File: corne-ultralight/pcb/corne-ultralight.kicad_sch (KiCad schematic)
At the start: 102 parts, among them J2 OLED, J7 OLED, SW1 SW_PUSH, SW10 SW_PUSH, SW11 SW_PUSH, SW12 SW_PUSH, SW13 SW_PUSH, SW14 SW_PUSH, SW15 SW_PUSH, SW16 SW_PUSH, SW17 SW_PUSH, SW18 SW_PUSH, SW19 SW_PUSH, SW2 SW_PUSH, SW20 SW_PUSH, SW21 SW_PUSH, SW22 SW_PUSH, SW23 SW_PUSH, SW24 SW_PUSH, SW25 SW_PUSH, SW26 SW_PUSH, SW27 SW_PUSH, SW28 SW_PUSH, SW29 SW_PUSH, SW3 SW_PUSH, SW30 SW_PUSH, SW31 SW_PUSH, SW32 SW_PUSH, SW33 SW_PUSH, SW34 SW_PUSH, SW35 SW_PUSH, SW36 SW_PUSH, SW37 SW_PUSH, SW38 SW_PUSH, SW39 SW_PUSH, SW4 SW_PUSH, SW40 SW_PUSH, SW41 SW_PUSH, SW42 SW_PUSH, SW5 SW_PUSH, SW6 SW_PUSH, SW7 SW_PUSH, SW8 SW_PUSH, SW9 SW_PUSH, U1 ProMicro, U2 ProMicro

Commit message: Right half changed to hotswaps
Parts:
- SW22, SW23, SW24, SW25, SW26, SW27, SW28, SW29, SW30, SW31, SW32, SW33, SW34, SW35, SW36, SW37, SW38, SW39, SW40, SW41: footprint gateron-ks27:gateron-ks27-choc-v1 -> kbd:CherryMX_Choc_Hotswap_BACKONLY_FLIPPED
- SW42: footprint gateron-ks27:gateron-ks27-choc-v1-1.5u -> kbd:CherryMX_Choc_Hotswap_1.5u_BACKONLY_FLIPPED

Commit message: Fixed flipped footprints
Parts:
- SW22, SW23, SW24, SW25, SW26, SW27, SW28, SW29, SW30, SW31, SW32, SW33, SW34, SW35, SW36, SW37, SW38, SW39, SW40, SW41: footprint kbd:CherryMX_Choc_Hotswap_BACKONLY_FLIPPED -> kbd:CherryMX_Choc_Hotswap_BACKONLY
- SW42: footprint kbd:CherryMX_Choc_Hotswap_1.5u_BACKONLY_FLIPPED -> kbd:CherryMX_Choc_Hotswap_1.5u_BACKONLY

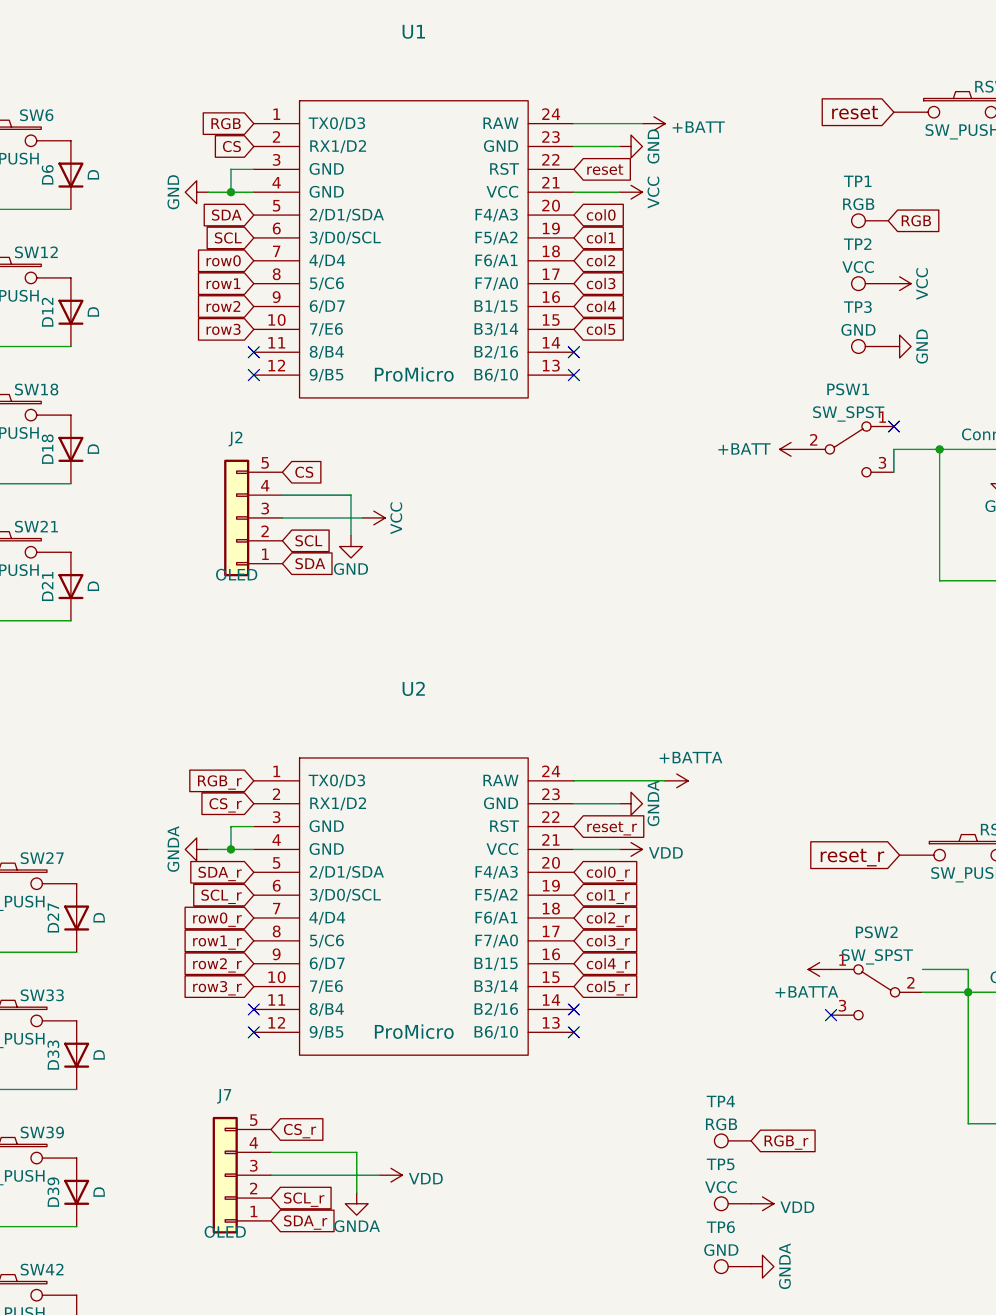
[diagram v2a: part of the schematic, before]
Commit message: Added XIAO footprint
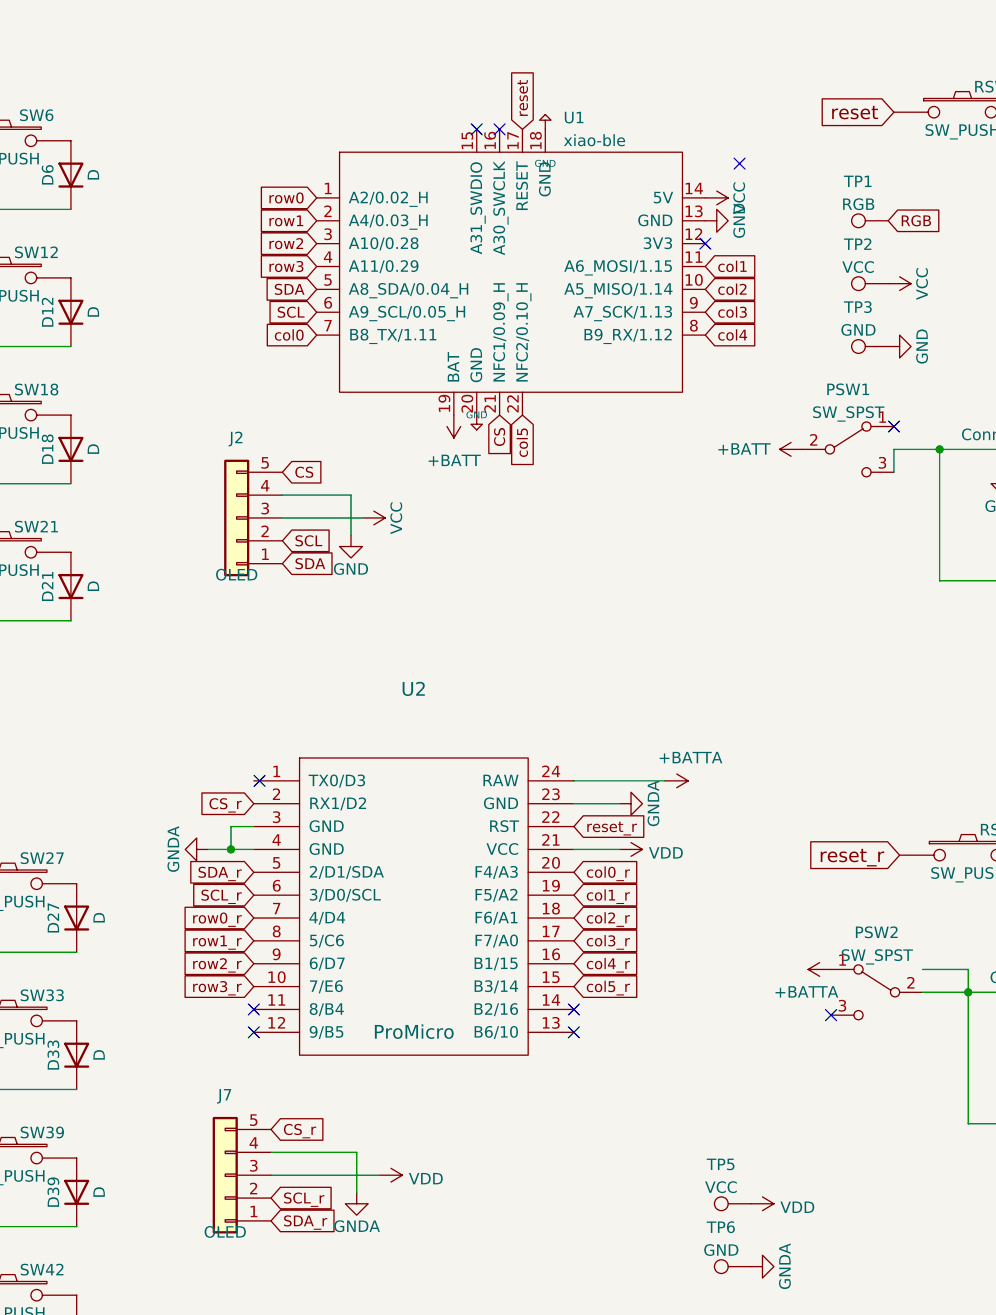
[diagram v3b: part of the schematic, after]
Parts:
- removed TP4: RGB, TestPoint:TestPoint_Pad_D1.5mm, symbol Connector:TestPoint
- removed U1: ProMicro, kbd:ProMicro_v3, symbol kbd:ProMicro
- added U1: xiao-ble, kleeb-mcu:xiao-ble-tht, symbol kleeb-mcu:xiao-ble
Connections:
- net +BATT: now also U1.19 (BAT)
- net CS: now also U1.21 (NFC1/0.09_H)
- net GND: now also U1.13 (GND)
- net SCL: now also U1.6 (A9_SCL/0.05_H)
- net SDA: now also U1.5 (A8_SDA/0.04_H)
- net VCC: now also U1.14 (5V)
- net col0: now also U1.7 (B8_TX/1.11)
- net col1: now also U1.11 (A6_MOSI/1.15)
- net col2: now also U1.10 (A5_MISO/1.14)
- net col3: now also U1.9 (A7_SCK/1.13)
- net col4: now also U1.8 (B9_RX/1.12)
- net col5: now also U1.22 (NFC2/0.10_H)
- net reset: now also U1.17 (RESET)
- net row0: now also U1.1 (A2/0.02_H)
- net row1: now also U1.2 (A4/0.03_H)
- net row2: now also U1.3 (A10/0.28)
- net row3: now also U1.4 (A11/0.29)
- net RGB_r: no longer names the net of U2.1 (TX0/D3)
- new net +5V: U1.18 (GND), U1.20 (GND)
- no-connect marks 10 -> 11

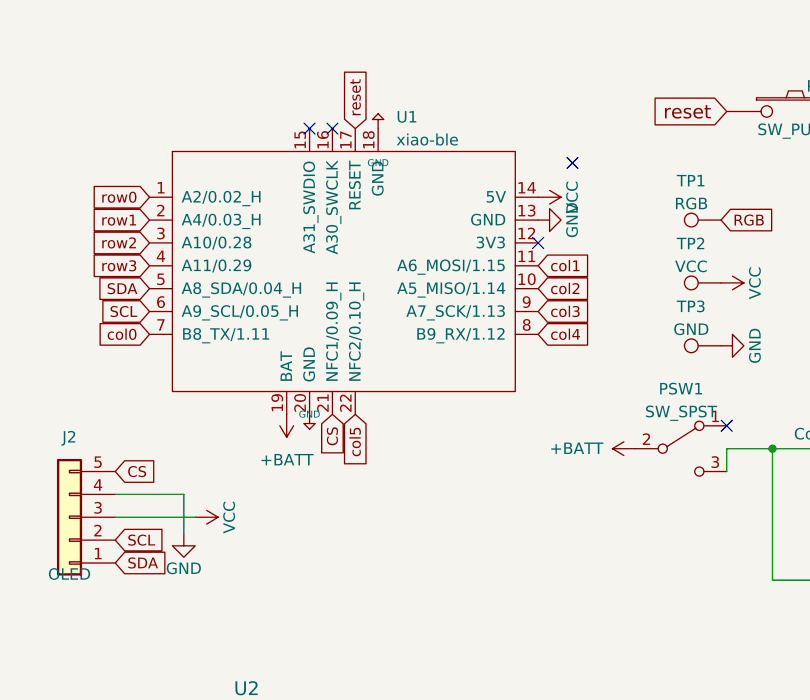
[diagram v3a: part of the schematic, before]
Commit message: Moved nice!view VCC to 3.3v
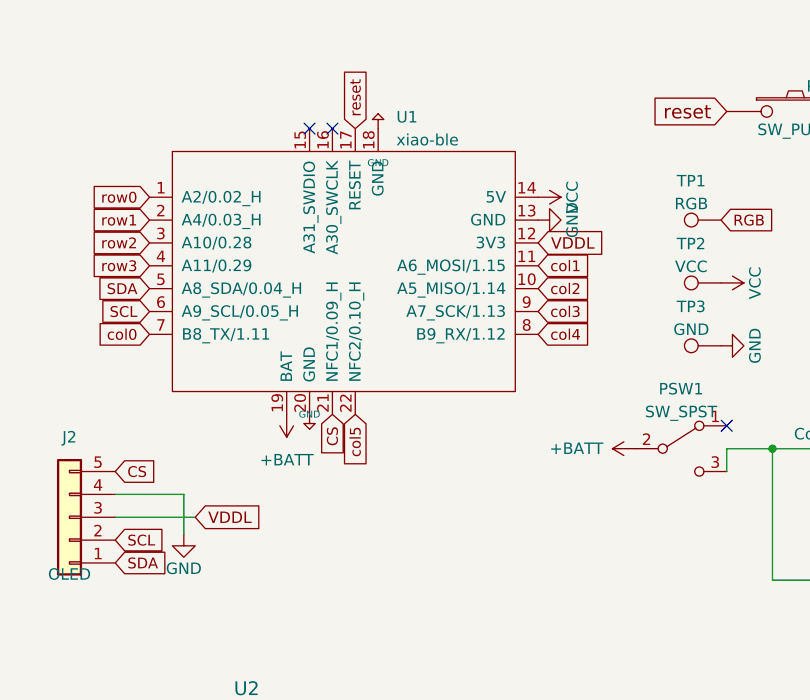
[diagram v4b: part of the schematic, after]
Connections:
- net VCC: no longer J2.3 (Pin_3)
- net VDDL: now reaches U1.12 (3V3)
- net VDDL: now also J2.3 (Pin_3)
- no-connect marks 11 -> 9
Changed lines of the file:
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@@
   (no_connect (at 167.64 22.86))
   (no_connect (at 211.455 55.88))
-  (no_connect (at 190.5 35.56))
   (no_connect (at 140.97 95.25))
-  (no_connect (at 194.31 26.67))
   (no_connect (at 140.335 123.19))
   (no_connect (at 175.895 123.19))
@@
     )
   )
+  (global_label "VDDL" (shape input) (at 190.5 35.56 0) (fields_autoplaced)
+    (effects (font (size 1.27 1.27)) (justify left))
+    (property "Intersheet References" "${INTERSHEET_REFS}" (id 0) (at 197.4809 35.4806 0)
+      (effects (font (size 1.27 1.27)) (justify left) hide)
+    )
+  )
   (global_label "col2" (shape input) (at 190.5 40.64 0) (fields_autoplaced)
     (effects (font (size 1.1938 1.1938)) (justify left))
@@
     )
   )
+  (global_label "VDDL" (shape input) (at 152.4 66.04 0) (fields_autoplaced)
+    (effects (font (size 1.27 1.27)) (justify left))
+    (property "Intersheet References" "${INTERSHEET_REFS}" (id 0) (at 159.3809 65.9606 0)
+      (effects (font (size 1.27 1.27)) (justify left) hide)
+    )
+  )
   (global_label "row1" (shape input) (at 147.32 33.02 180) (fields_autoplaced)
     (effects (font (size 1.1938 1.1938)) (justify right))
@@
     )
     (property "Datasheet" "" (id 3) (at 151.13 67.945 0)
-      (effects (font (size 1.27 1.27)) hide)
-    )
-    (pin "1")
-  )
-  (symbol (lib_id "power:VCC") (at 152.4 66.04 270) (unit 1)
-    (in_bom yes) (on_board yes)
-    (property "Reference" "#PWR018" (id 0) (at 148.59 66.04 0)
-      (effects (font (size 1.27 1.27)) hide)
-    )
-    (property "Value" "VCC" (id 1) (at 156.21 66.04 0))
-    (property "Footprint" "" (id 2) (at 152.4 66.04 0)
-      (effects (font (size 1.27 1.27)) hide)
-    )
-    (property "Datasheet" "" (id 3) (at 152.4 66.04 0)
       (effects (font (size 1.27 1.27)) hide)
     )
@@
       (reference "#PWR014") (unit 1) (value "GNDA") (footprint "")
     )
-    (path "/00000000-0000-0000-0000-00005a923dd7"
-      (reference "#PWR018") (unit 1) (value "VCC") (footprint "")
-    )
     (path "/00000000-0000-0000-0000-00005a92390a"
